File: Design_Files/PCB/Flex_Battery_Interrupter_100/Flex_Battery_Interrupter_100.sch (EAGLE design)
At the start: 3 parts

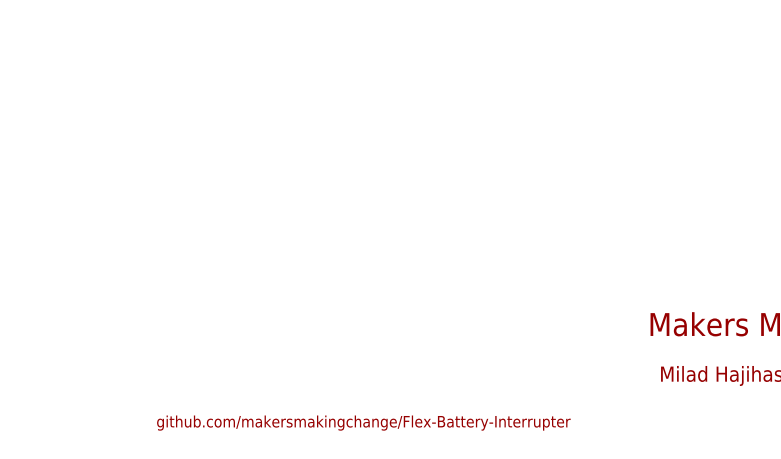
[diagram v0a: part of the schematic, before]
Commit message: Renamed the Flex Battery Interrupter to Flex Battery Interrupter 100 (100mm). Model:100,Version:1.00
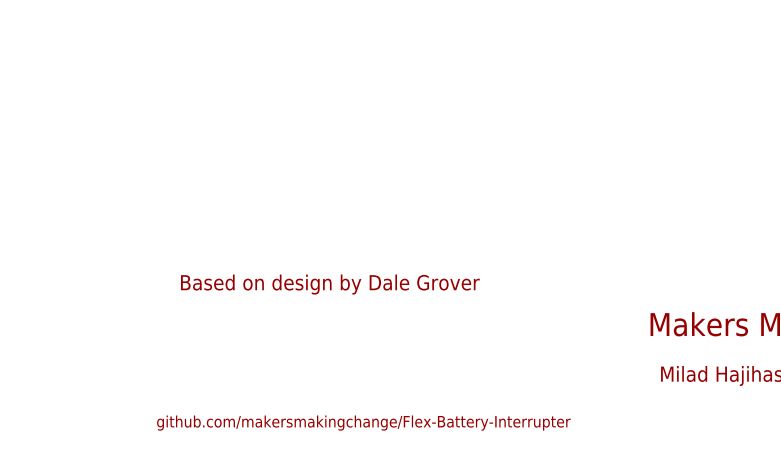
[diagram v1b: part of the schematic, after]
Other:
- note added: "Based on design by Dale Grover"
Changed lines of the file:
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@@
 <text x="241.3" y="-55.88" size="1.27" layer="94">github.com/makersmakingchange/Flex-Battery-Interrupter</text>
 <text x="297.18" y="-50.8" size="1.6764" layer="94">Milad Hajihassan</text>
+<text x="243.84" y="-40.64" size="1.6764" layer="94">Based on design by Dale Grover</text>
 </plain>
 <instances>
 <instance part="FRAME1" gate="G$1" x="-48.26" y="-60.96" smashed="yes">
-<attribute name="DRAWING_NAME" x="295.91" y="-40.64" size="2.1844" layer="94"/>
+<attribute name="DRAWING_NAME" x="295.91" y="-40.64" size="1.9304" layer="94"/>
 <attribute name="SHEET" x="309.245" y="-55.88" size="2.54" layer="94"/>
 </instance>
